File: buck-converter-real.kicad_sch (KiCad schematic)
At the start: 30 parts

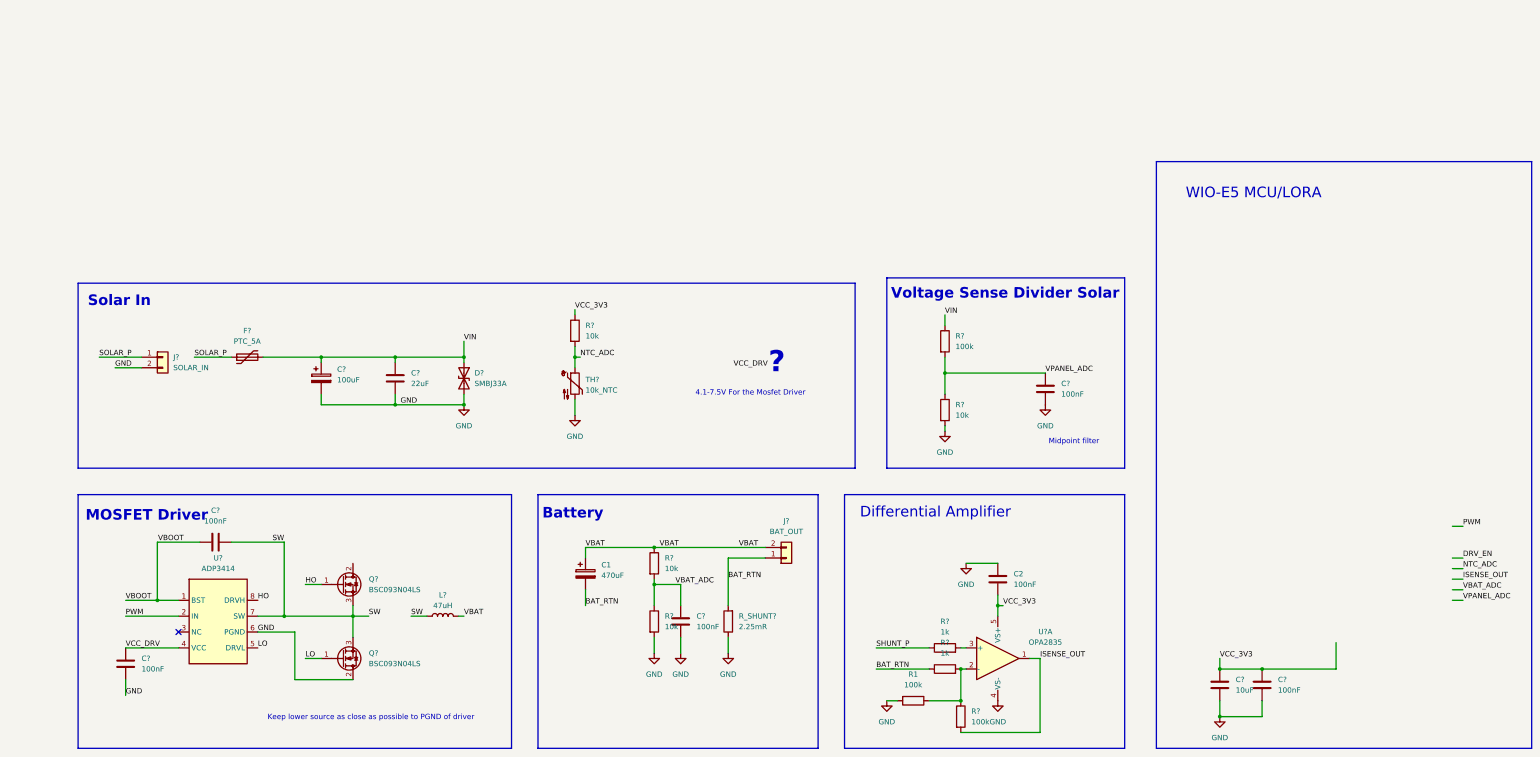
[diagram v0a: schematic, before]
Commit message: Add layout and new components
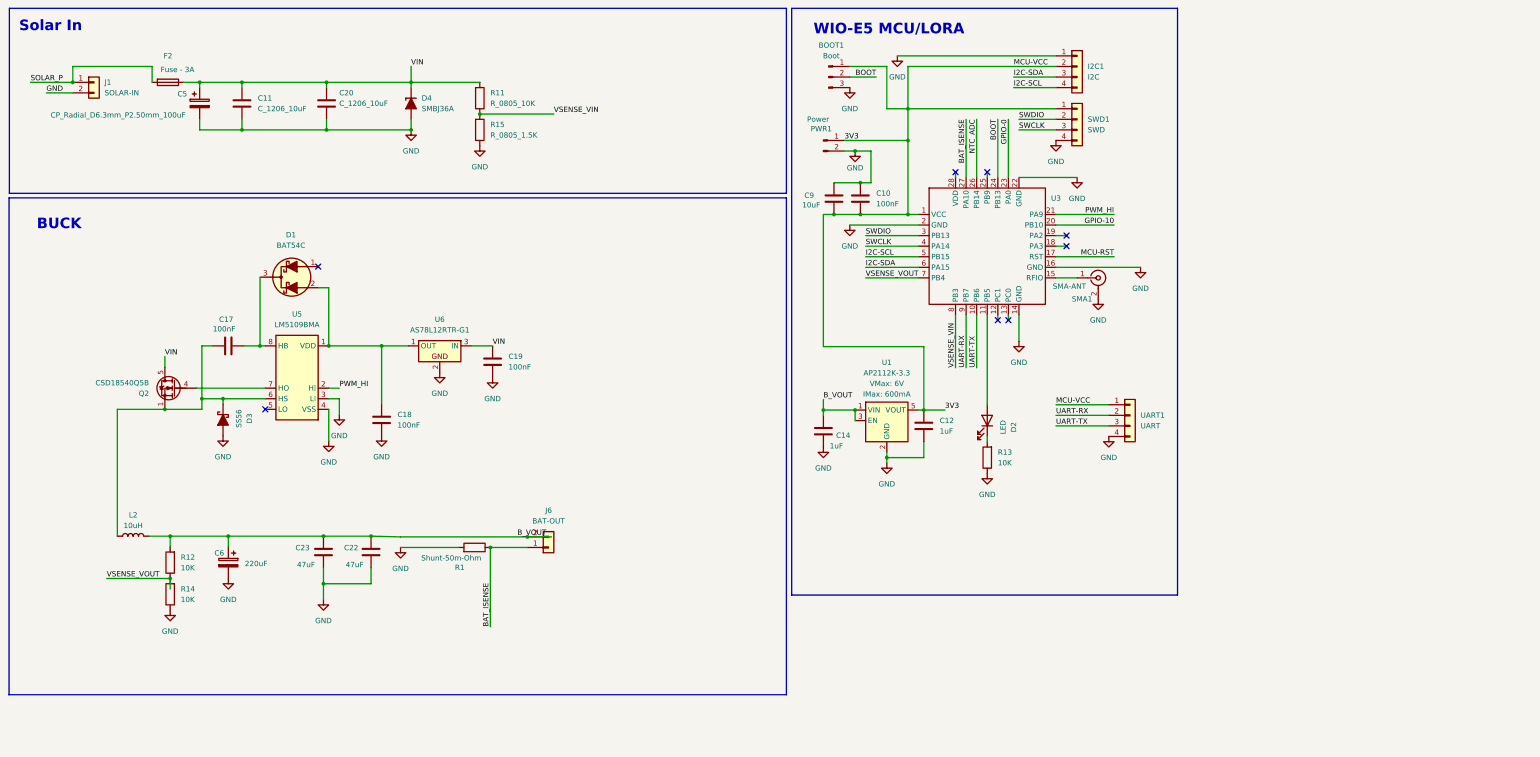
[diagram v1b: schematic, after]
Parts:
- removed C1: 470uF, Capacitor_SMD:CP_Elec_10x10, symbol Device:C_Polarized
- removed C2, C? (x5): 100nF, Capacitor_SMD:C_0603_1608Metric, symbol Device:C
- removed C?: 10uF, Capacitor_SMD:C_0603_1608Metric, symbol Device:C
- removed C?: 100uF, Capacitor_SMD:CP_Elec_8x10, symbol Device:C_Polarized
- removed C?: 22uF, Capacitor_SMD:C_1206_3216Metric, symbol Device:C
- removed D?: SMBJ33A, Diode_SMD:D_SMB, symbol Device:D_TVS
- removed F?: PTC_5A, Fuse:Fuse_1206_3216Metric, symbol Device:Polyfuse
- removed J?: BAT_OUT, Connector_PinHeader_2.54mm:PinHeader_1x02_P2.54mm_Vertical, symbol Connector_Generic:Conn_01x02
- removed L?: 47uH, Inductor_SMD:L_Coilcraft_MSS1514V-XXX, symbol Device:L
- removed Q? (x2): BSC093N04LS, Package_SON:Infineon_PG-TDSON-8_6.15x5.15mm, symbol Transistor_FET:Q_NMOS_GDS
- removed R1, R? (x2): 100k, Resistor_SMD:R_0603_1608Metric, symbol Device:R
- removed R? (x4): 10k, Resistor_SMD:R_0603_1608Metric, symbol Device:R
- removed R? (x2): 1k, Resistor_SMD:R_0603_1608Metric, symbol Device:R
- removed R_SHUNT?: 2.25mR, Resistor_SMD:R_2512_6332Metric, symbol Device:R
- removed TH?: 10k_NTC, Resistor_SMD:R_0603_1608Metric, symbol Device:Thermistor_NTC
- removed U?: ADP3414, Package_SO:SOIC-8-N7_3.9x4.9mm_P1.27mm, symbol Driver_FET:IR2104
- removed U?: OPA2835, Package_SO:VSSOP-8_3x3mm_P0.65mm, symbol Amplifier_Operational:OPA2134
- added BOOT1: Boot, Connector_PinSocket_2.54mm:PinSocket_1x03_P2.54mm_Vertical, symbol Connector:Conn_01x03_Pin
- added C10: 100nF, Capacitor_SMD:C_0603_1608Metric, symbol Device:C
- added C11, C20: C_1206_10uF, PCM_Capacitor_SMD_AKL:C_1206_3216Metric, symbol PCM_Capacitor_AKL:C_1206
- added C12, C14: 1uF, PCM_Capacitor_SMD_AKL:C_0805_2012Metric, symbol PCM_Capacitor_AKL:C_0805
- added C17, C18, C19: 100nF, PCM_Capacitor_SMD_AKL:C_0805_2012Metric, symbol PCM_Capacitor_AKL:C_0805
- added C22, C23: 47uF, PCM_Capacitor_SMD_AKL:C_1206_3216Metric, symbol PCM_Capacitor_AKL:C_1206
- added C5: CP_Radial_D6.3mm_P2.50mm_100uF, PCM_Capacitor_THT_AKL:CP_Radial_D6.3mm_P2.50mm, symbol PCM_Capacitor_AKL:CP_Radial_D6.3mm_P2.50mm
- added C6: 220uF, PCM_Capacitor_THT_AKL:CP_Radial_D6.3mm_P2.50mm, symbol PCM_Capacitor_AKL:CP_Radial_D6.3mm_P2.50mm
- added C9: 10uF, Capacitor_SMD:C_0603_1608Metric, symbol Device:C
- added D1: BAT54C, PCM_Package_TO_SOT_SMD_AKL:SOT-23, symbol PCM_Diode_Schottky_AKL:BAT54C
- added D2: LED, LED_SMD:LED_0603_1608Metric_Pad1.05x0.95mm_HandSolder, symbol Device:LED
- added D3: SS56, PCM_Diode_SMD_AKL:D_SMC, symbol PCM_Diode_Schottky_AKL:SS56
- added D4: SMBJ36A, Diode_THT:D_DO-201_P5.08mm_Vertical_CathodeUp, symbol PCM_Diode_TVS_AKL:SMBJ36A
- added F2: Fuse - 3A, Fuse:Fuse_1206_3216Metric, symbol Device:Fuse
- added I2C1: I2C, Connector_PinSocket_2.54mm:PinSocket_1x04_P2.54mm_Vertical, symbol PCM_SparkFun-Connector:Conn_01x04_P2.54mm_Header_Horizontal_SMD
- added J6: BAT-OUT, Connector_PinHeader_2.54mm:PinHeader_1x02_P2.54mm_Vertical, symbol Connector_Generic:Conn_01x02
- added L2: 10uH, Inductor_SMD:L_10.4x10.4_H4.8, symbol Device:L
- added PWR1: Power, Connector_PinSocket_2.54mm:PinSocket_1x02_P2.54mm_Vertical, symbol Connector:Conn_01x02_Pin
- added Q2: CSD18540Q5B, Package_TO_SOT_SMD:TDSON-8-1, symbol Transistor_FET:CSD18540Q5B
- added R1: Shunt-50m-Ohm, PCM_Resistor_SMD_AKL:R_2512_6332Metric, symbol PCM_Resistor_AKL:R_2512
- added R11: R_0805_10K, PCM_Resistor_SMD_AKL:R_0805_2012Metric, symbol PCM_Resistor_AKL:R_0805
- added R12, R13, R14: 10K, PCM_Resistor_SMD_AKL:R_0805_2012Metric, symbol PCM_Resistor_AKL:R_0805
- added R15: R_0805_1.5K, PCM_Resistor_SMD_AKL:R_0805_2012Metric, symbol PCM_Resistor_AKL:R_0805
- added SMA1: SMA-ANT, Connector_Coaxial:SMA_Samtec_SMA-J-P-H-ST-EM1_EdgeMount, symbol Connector:Conn_Coaxial
- added SWD1: SWD, Connector_PinSocket_2.54mm:PinSocket_1x04_P2.54mm_Vertical, symbol PCM_SparkFun-Connector:Conn_01x04_P2.54mm_Header_Horizontal_SMD
- added U1: AP2112K-3.3, PCM_SparkFun-Semiconductor-Standard:SOT23-5, symbol PCM_SparkFun-Regulator:AP2112K-3.3
- added U3: (no value), LoRa-E5:LoRa-E5, symbol wio-e5:WIO-E5
- added U5: LM5109BMA, Package_SO:SOIC-8_3.9x4.9mm_P1.27mm, symbol Driver_FET:LM5109BMA
- added U6: AS78L12RTR-G1, OptoDevice:Broadcom_APDS-9160-003, symbol PCM_Voltage_Regulator_AKL:AS78L12RTR-G1
- added UART1: UART, Connector_PinSocket_2.54mm:PinSocket_1x04_P2.54mm_Vertical, symbol PCM_SparkFun-Connector:Conn_01x04_P2.54mm_Header_Horizontal_SMD
- J1: renamed from J?; value SOLAR_IN -> SOLAR-IN
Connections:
- net GND: now also BOOT1.3 (Pin_3), C10.1, C11.2, C12.2, C14.2, C18.2, C19.2, C20.2, C22.2, C23.2, C5.2, C6.2, C9.1, D3.2 (A), D4.2 (A), I2C1.1 (Pin_1), PWR1.2 (Pin_2), R1.1, R13.2, R14.2, R15.2, SMA1.2 (Ext), SWD1.4 (Pin_4), U1.2 (GND), U3.14 (GND), U3.16 (GND), U3.2 (GND), U3.22 (GND), U5.3 (LI), U5.4 (VSS), U6.2, UART1.4 (Pin_4)
- net NTC_ADC: now also U3.26 (PB14)
- net SOLAR_P: now also F2.2
- net VIN: now also C11.1, C19.1, C20.1, C5.1, D4.1 (K), F2.1, Q2.5 (D), R11.1, U6.3 (IN)
- new net: C18.1, D1.2 (A1), U5.1 (VDD), U6.1 (OUT)
- new net: C17.1, D3.1 (K), L2.2, Q2.1 (S), Q2.2 (S), Q2.3 (S), U5.6 (HS)
- new net: D2.1 (K), R13.1
- new net: D2.2 (A), U3.11 (PB5)
- new net: SMA1.1 (In), U3.15 (RFIO)
- new net: C17.2, D1.3 (K), U5.8 (HB)
- new net: Q2.4 (G), U5.7 (HO)
- new net 3V3: BOOT1.1 (Pin_1), C10.2, C12.1, C9.2, I2C1.2 (Pin_2), PWR1.1 (Pin_1), SWD1.1 (Pin_1), U1.5 (VOUT), U3.1 (VCC), UART1.1 (Pin_1)
- new net BAT_ISENSE: J6.1 (Pin_1), R1.2, U3.27 (PA10)
- new net BOOT: BOOT1.2 (Pin_2), U3.24 (PB13)
- new net B_VOUT: C14.1, C22.1, C23.1, C6.1, J6.2 (Pin_2), L2.1, R12.1, U1.1 (VIN), U1.3 (EN)
- new net GPIO-0: U3.23 (PA0)
- new net GPIO-10: U3.20 (PB10)
- new net I2C-SCL: I2C1.4 (Pin_4), U3.5 (PB15)
- new net I2C-SDA: I2C1.3 (Pin_3), U3.6 (PA15)
- new net MCU-RST: U3.17 (RST)
- new net PWM_HI: U3.21 (PA9), U5.2 (HI)
- new net SWCLK: SWD1.3 (Pin_3), U3.4 (PA14)
- new net SWDIO: SWD1.2 (Pin_2), U3.3 (PB13)
- new net UART-RX: U3.9 (PB7), UART1.2 (Pin_2)
- new net UART-TX: U3.10 (PB6), UART1.3 (Pin_3)
- new net VSENSE_VIN: R11.2, R15.1, U3.8 (PB3)
- new net VSENSE_VOUT: R12.2, R14.1, U3.7 (PB4)
- no-connect marks 1 -> 8
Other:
- note added: "BUCK"
- note removed: "4.1-7.5V For the Mosfet Driver"
- note removed: "?"
- note removed: "Battery"
- note removed: "Differential Amplifier"
- note removed: "Keep lower source as close as possible to PGND of driver"
- note removed: "MOSFET Driver"
- note removed: "Midpoint filter"
- note removed: "Voltage Sense Divider Solar"
- moved on the sheet: J1

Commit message: Update PCB
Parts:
- removed PWR1: Power, Connector_PinSocket_2.54mm:PinSocket_1x02_P2.54mm_Vertical, symbol Connector:Conn_01x02_Pin
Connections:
- net 3V3: now also UART1.4 (Pin_4); no longer UART1.1 (Pin_1)
- net GND: now also UART1.1 (Pin_1); no longer UART1.4 (Pin_4)
- net UART-RX: now also UART1.3 (Pin_3); no longer UART1.2 (Pin_2)
- net UART-TX: now also UART1.2 (Pin_2); no longer UART1.3 (Pin_3)
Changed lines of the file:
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@@
 	(wire
 		(pts
+			(xy 276.86 128.27) (xy 289.56 128.27)
+		)
+		(stroke
+			(width 0)
+			(type default)
+		)
+	)
+	(wire
+		(pts
 			(xy 71.6541 119.2066) (xy 76.7341 119.2066)
 		)
@@
 	(wire
 		(pts
-			(xy 276.86 120.65) (xy 289.56 120.65)
+			(xy 273.05 120.65) (xy 289.56 120.65)
 		)
 		(stroke
@@
 		)
 	)
-	(label "MCU-VCC"
-		(at 276.86 120.65 0)
-		(effects
-			(font
-				(size 1.27 1.27)
-			)
-			(justify left bottom)
-		)
-	)
 	(label "VSENSE_VIN"
 		(at 252.73 111.76 90)
@@
 		)
 	)
-	(label "UART-RX"
-		(at 276.86 123.19 0)
-		(effects
-			(font
-				(size 1.27 1.27)
-			)
-			(justify left bottom)
-		)
-	)
 	(label "PWM_HI"
 		(at 104.6741 116.6666 0)
@@
 		)
 	)
+	(label "UART-RX"
+		(at 276.86 125.73 0)
+		(effects
+			(font
+				(size 1.27 1.27)
+			)
+			(justify left bottom)
+		)
+	)
 	(label "UART-TX"
 		(at 257.81 111.76 90)
@@
 		)
 	)
-	(label "UART-TX"
-		(at 276.86 125.73 0)
+	(label "BOOT"
+		(at 262.89 52.07 270)
 		(effects
 			(font
 				(size 1.27 1.27)
 			)
-			(justify left bottom)
+			(justify right bottom)
 		)
 	)
-	(label "BOOT"
-		(at 262.89 52.07 270)
+	(label "SWCLK"
+		(at 267.97 54.61 0)
 		(effects
 			(font
 				(size 1.27 1.27)
 			)
-			(justify right bottom)
+			(justify left bottom)
 		)
 	)
-	(label "SWCLK"
-		(at 267.97 54.61 0)
+	(label "UART-TX"
+		(at 276.86 123.19 0)
 		(effects
 			(font
@@
 		)
 	)
+	(label "MCU-VCC"
+		(at 276.86 128.27 0)
+		(effects
+			(font
+				(size 1.27 1.27)
+			)
+			(justify left bottom)
+		)
+	)
 	(label "B_VOUT"
 		(at 154.4059 152.4 180)
@@
 	)
 	(symbol
-		(lib_id "Connector:Conn_01x02_Pin")
-		(at 220.98 57.15 0)
-		(unit 1)
-		(body_style 1)
-		(exclude_from_sim no)
-		(in_bom yes)
-		(on_board yes)
-		(in_pos_files yes)
-		(dnp no)
-		(property "Reference" "PWR1"
-			(at 220.472 54.356 0)
-			(show_name no)
-			(do_not_autoplace no)
-			(effects
-				(font
-					(size 1.27 1.27)
-				)
-			)
-		)
-		(property "Value" "Power"
-			(at 219.71 52.07 0)
-			(show_name no)
-			(do_not_autoplace no)
-			(effects
-				(font
-					(size 1.27 1.27)
-				)
-			)
-		)
-		(property "Footprint" "Connector_PinSocket_2.54mm:PinSocket_1x02_P2.54mm_Vertical"
-			(at 220.98 57.15 0)
-			(hide yes)
-			(show_name no)
-			(do_not_autoplace no)
-			(effects
-				(font
-					(size 1.27 1.27)
-				)
-			)
-		)
-		(property "Datasheet" ""
-			(at 220.98 57.15 0)
-			(hide yes)
-			(show_name no)
-			(do_not_autoplace no)
-			(effects
-				(font
-					(size 1.27 1.27)
-				)
-			)
-		)
-		(property "Description" "Generic connector, single row, 01x02, script generated"
-			(at 220.98 57.15 0)
-			(hide yes)
-			(show_name no)
-			(do_not_autoplace no)
-			(effects
-				(font
-					(size 1.27 1.27)
-				)
-			)
-		)
-		(pin "1"
-		)
-		(pin "2"
-		)
-		(instances
-			(project "buck-converter-real"
-				(path "/cbc98a1b-0533-4e8d-81af-0515d3e50555"
-					(reference "PWR1")
-					(unit 1)
-				)
-			)
-		)
-	)
-	(symbol
 		(lib_id "PCM_Capacitor_AKL:C_0805")
 		(at 245.11 125.73 0)
@@
 	(symbol
 		(lib_id "power:GND")
-		(at 289.56 128.27 0)
-		(unit 1)
-		(body_style 1)
-		(exclude_from_sim no)
-		(in_bom yes)
-		(on_board yes)
-		(in_pos_files yes)
-		(dnp no)
-		(fields_autoplaced yes)
-		(property "Reference" "#PWR028"
-			(at 289.56 134.62 0)
-			(hide yes)
-			(show_name no)
-			(do_not_autoplace no)
-			(effects
-				(font
-					(size 1.27 1.27)
-				)
-			)
-		)
-		(property "Value" "GND"
-			(at 289.56 133.35 0)
-			(show_name no)
-			(do_not_autoplace no)
-			(effects
-				(font
-					(size 1.27 1.27)
-				)
-			)
-		)
-		(property "Footprint" ""
-			(at 289.56 128.27 0)
-			(hide yes)
-			(show_name no)
-			(do_not_autoplace no)
-			(effects
-				(font
-					(size 1.27 1.27)
-				)
-			)
-		)
-		(property "Datasheet" ""
-			(at 289.56 128.27 0)
-			(hide yes)
-			(show_name no)
-			(do_not_autoplace no)
-			(effects
-				(font
-					(size 1.27 1.27)
-				)
-			)
-		)
-		(property "Description" "Power symbol creates a global label with name \"GND\" , ground"
-			(at 289.56 128.27 0)
-			(hide yes)
-			(show_name no)
-			(do_not_autoplace no)
-			(effects
-				(font
-					(size 1.27 1.27)
-				)
-			)
-		)
-		(pin "1"
-		)
-		(instances
-			(project "buck-converter-real"
-				(path "/cbc98a1b-0533-4e8d-81af-0515d3e50555"
-					(reference "#PWR028")
-					(unit 1)
-				)
-			)
-		)
-	)
-	(symbol
-		(lib_id "power:GND")
 		(at 260.35 137.16 0)
 		(unit 1)
@@
 					(unit 1)
 				)
+			)
+		)
+	)
+	(symbol
+		(lib_id "power:GND")
+		(at 273.05 120.65 0)
+		(unit 1)
+		(body_style 1)
+		(exclude_from_sim no)
+		(in_bom yes)
+		(on_board yes)
+		(in_pos_files yes)
+		(dnp no)
+		(fields_autoplaced yes)
+		(property "Reference" "#PWR028"
+			(at 273.05 127 0)
+			(hide yes)
+			(show_name no)
+			(do_not_autoplace no)
+			(effects
+				(font
+					(size 1.27 1.27)
+				)
+			)
+		)
+		(property "Value" "GND"
+			(at 273.05 125.73 0)
+			(show_name no)
+			(do_not_autoplace no)
+			(effects
+				(font
+					(size 1.27 1.27)
+				)
+			)
+		)
+		(property "Footprint" ""
+			(at 273.05 120.65 0)
+			(hide yes)
+			(show_name no)
+			(do_not_autoplace no)
+			(effects
+				(font
+					(size 1.27 1.27)
+				)
+			)
+		)
+		(property "Datasheet" ""
+			(at 273.05 120.65 0)
+			(hide yes)
+			(show_name no)
+			(do_not_autoplace no)
+			(effects
+				(font
+					(size 1.27 1.27)
+				)
+			)
+		)
+		(property "Description" "Power symbol creates a global label with name \"GND\" , ground"
+			(at 273.05 120.65 0)
+			(hide yes)
+			(show_name no)
+			(do_not_autoplace no)
+			(effects
+				(font
+					(size 1.27 1.27)
+				)
+			)
+		)
+		(pin "1"
+		)
+		(instances
+			(project "buck-converter-real"
+				(path "/cbc98a1b-0533-4e8d-81af-0515d3e50555"
+					(reference "#PWR028")
+					(unit 1)
+				)
